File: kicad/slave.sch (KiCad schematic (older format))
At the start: 53 parts, among them IC1 ATMEGA8A-P, J1 DB9, K1 CONN_3, K2 CONN_3, K3 CONN_3, K4 CONN_3, P2 CONN_4, Q1 BC547, Q2 BC547, Q3 BC547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

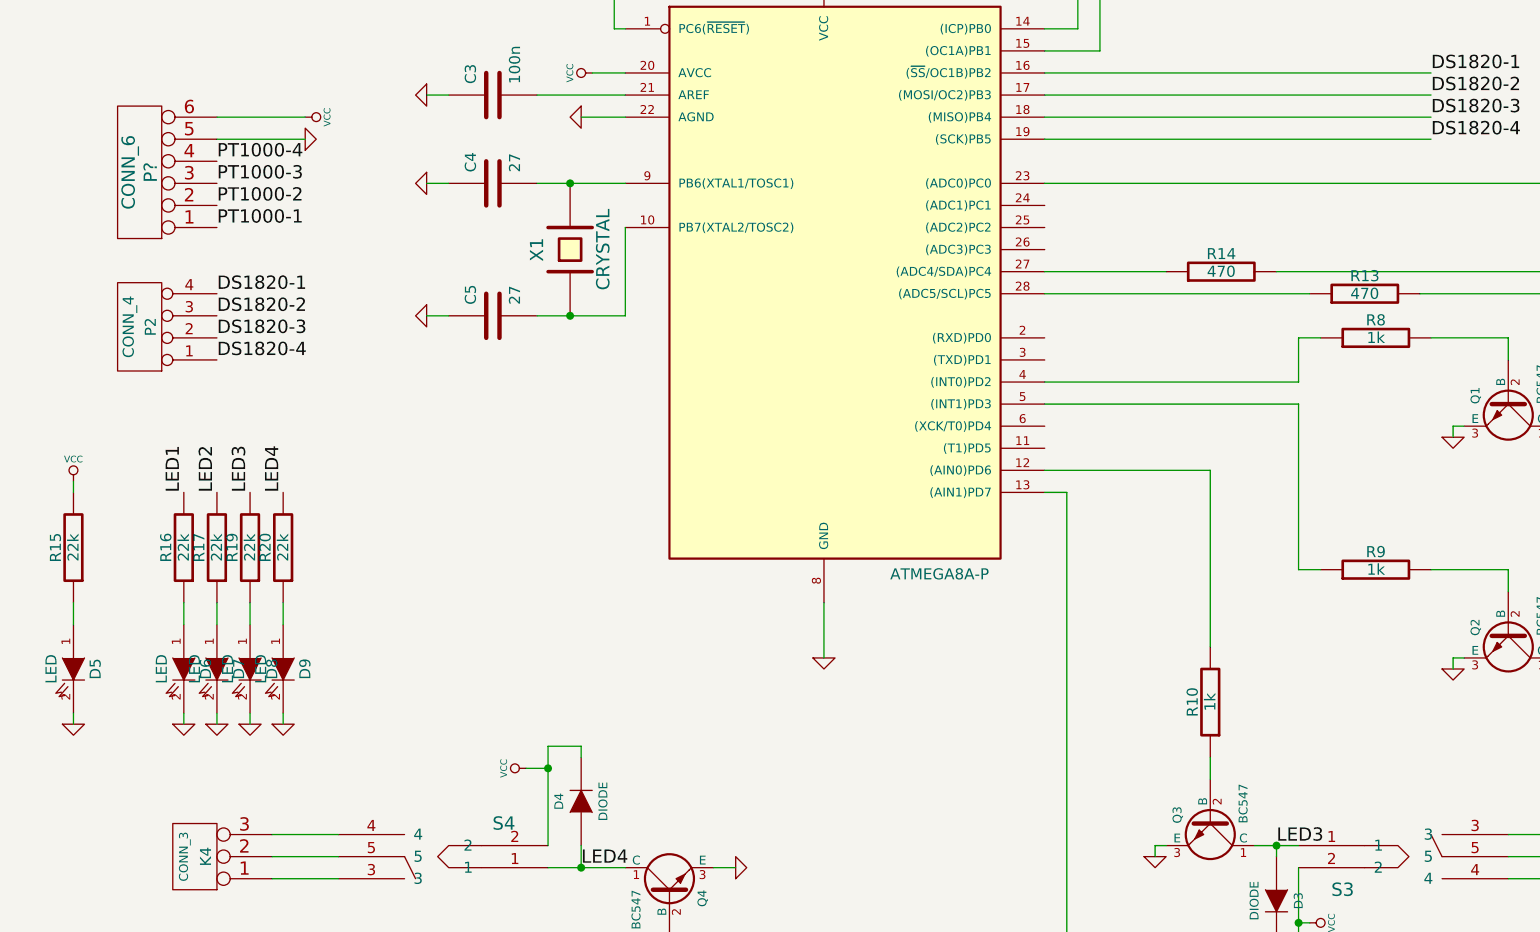
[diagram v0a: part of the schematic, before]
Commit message: Updated schematic, moved kicad files out of the way
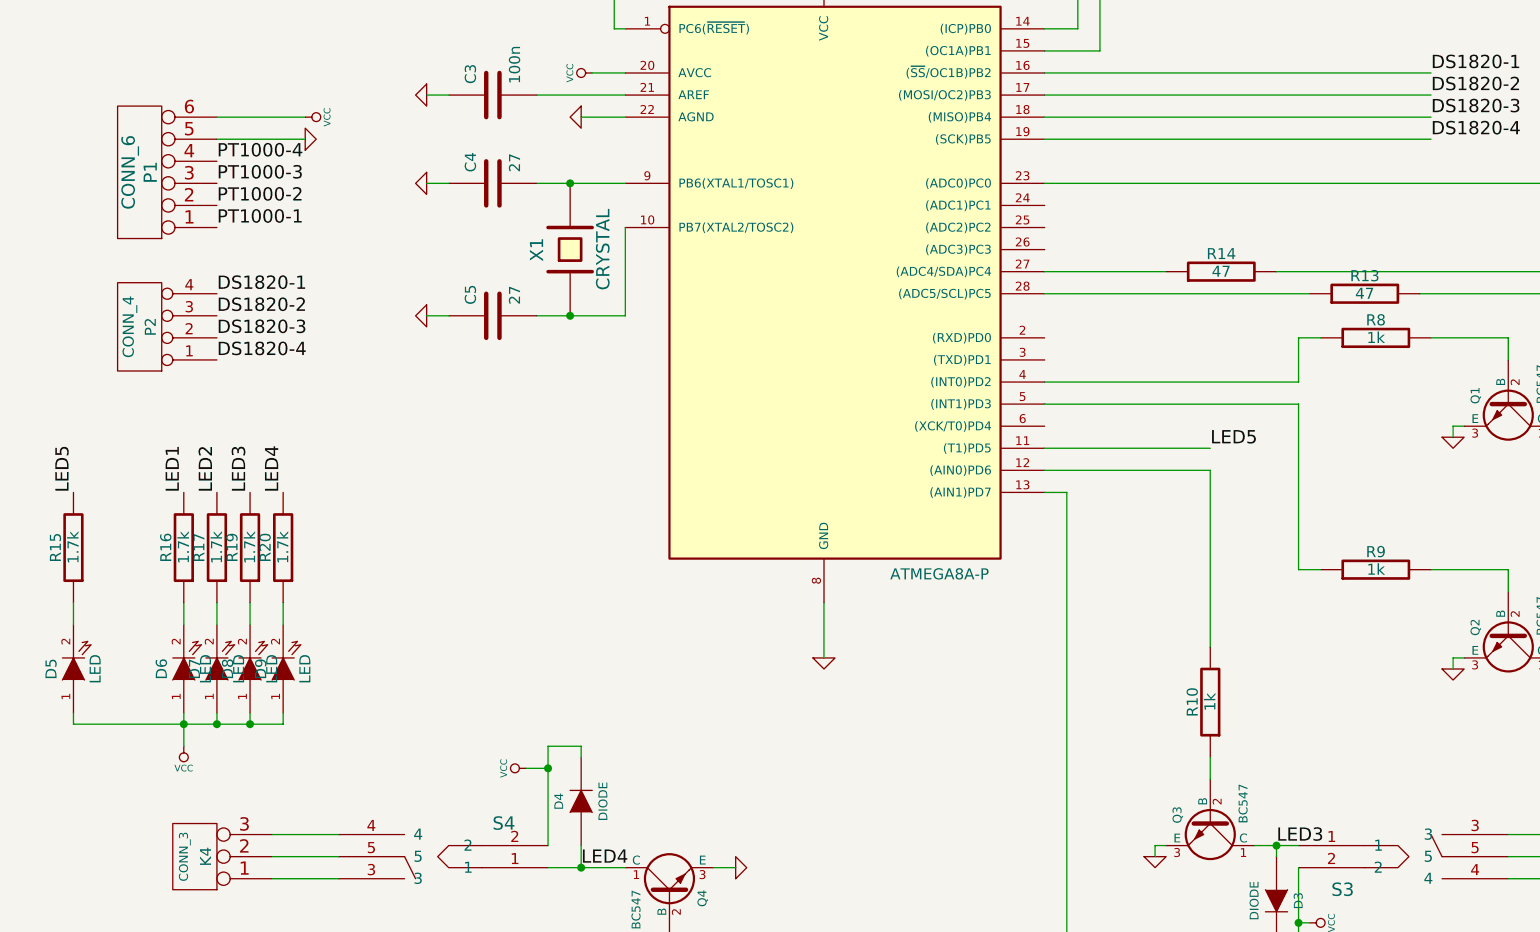
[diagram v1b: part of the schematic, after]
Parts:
- R13, R14: value 470 -> 47
- R15, R16, R17, R19, R20: value 22k -> 1.7k
- gave numbers to parts that had none: 1
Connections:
- net GND: no longer D5.2 (K), D6.2 (K), D7.2 (K), D8.2 (K), D9.2 (K)
- net VCC: now also D5.1 (A), D6.1 (A), D7.1 (A), D8.1 (A), D9.1 (A); no longer R15.2
- net LED5: now reaches IC1.11 ((T1)PD5)
- net LED5: now also R15.2
- net at R15.1: now also D5.2 (K); no longer D5.1 (A)
- net at R16.1: now also D6.2 (K); no longer D6.1 (A)
- net at R17.1: now also D7.2 (K); no longer D7.1 (A)
- net at R19.1: now also D8.2 (K); no longer D8.1 (A)
- net at R20.1: now also D9.2 (K); no longer D9.1 (A)
